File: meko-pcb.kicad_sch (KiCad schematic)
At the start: 75 parts, among them IC1 AS5600-ASOM, IC2 TCAL9538RSVR, J1 GDEY0154D67, J2 MEM2090-00-145-00-A, M1 Motor_DC, Q1 SS8050, Q2 SS8050, Q3 SS8050, Q4 Si1308EDL, SW1 SW_Push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

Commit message: added titles to sheets
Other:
- title: (none) -> ROOT
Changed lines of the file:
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@@
 	(generator_version "9.0")
 	(paper "A3")
+	(title_block
+		(title "ROOT")
+	)
 	(rectangle
 		(start 118.11 86.36)

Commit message: small fixes
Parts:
- added D13: MBR0530, Diode_SMD:D_SOD-123, symbol Diode:MBR0530
- D1: footprint Diode_THT:D_DO-41_SOD81_P3.81mm_Vertical_AnodeUp -> Diode_SMD:D_SMA
- R10, R11: value 10k -> 1.2k
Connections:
- net AUDIO_DATA1: no longer U1.35 (GPIO21)
- net AUDIO_DATA_2: no longer U1.34 (GPIO22)
- net AUDIO_DATA_CLK: now also D13.1 (K); no longer Q2.3 (C)
- net BTN_SIDE_L: now also U1.34 (GPIO22); no longer IC2.5 (P3)
- net BTN_SIDE_R: now also U1.35 (GPIO21); no longer IC2.10 (P7)
- net I2C_1_SCL renamed I2C_SCL
- net I2C_1_SDA renamed I2C_SDA
- new net: D13.2 (A), Q2.3 (C)
- new net PWR_EN3V3AVDD: IC2.10 (P7)
- no-connect marks 6 -> 7
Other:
- sheet power ports: added EN3V3AVDD; removed none

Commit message: fuel gauge ic
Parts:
- C1, C10, C11, C12, C13, C14, C15, C16, C17, C18, C19, C2, C20, C21, C22, C3, C4, C5, C6, C7, C8, C9: footprint (none) -> Capacitor_SMD:C_0402_1005Metric
- IC1: footprint SOIC127P600X175-8N -> AS5600-ASOM:SOIC127P600X175-8N
- IC2: footprint QFN40P180X260X55-16N -> TCAL9538RSVR:QFN40P180X260X55-16N
- J1: footprint FH34SRJ24S05SH99 -> FH34SRJ-24S-0.5SH(99):FH34SRJ24S05SH99
- R1, R12, R13, R14, R15, R2, R3, R4, R5, R6, R7, R8, R9: footprint (none) -> Resistor_SMD:R_0402_1005Metric
- R10, R11: value 1.2k -> 10k; footprint (none) -> Resistor_SMD:R_0402_1005Metric
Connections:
- net AUDIO_SCL is gone; now on net AUDIO_DATA1: U1.15 (GPIO25/ADC2_CH8/DAC_1)
- net AUDIO_SDA is gone; now on net AUDIO_DATA1: U1.16 (GPIO26/ADC2_CH9/DAC_2)
- net AUDIO_DATA_CLK: no longer C7.1, D13.1 (K), SW7.2, U1.23 (GPIO0/BOOT/ADC2_CH1)
- net LED: now also U1.27 (SD_DATA_0/GPIO7); no longer U1.7 (SENSOR_VN/GPIO39/ADC1_CH3)
- net MEM_COM: now also U1.7 (SENSOR_VN/GPIO39/ADC1_CH3); no longer U1.27 (SD_DATA_0/GPIO7)
- net PWR_FUEL_GPOUT: now reaches IC2.5 (P3)
- new net AUDIO_DATA_CLK/BOOT: C7.1, D13.1 (K), SW7.2, U1.23 (GPIO0/BOOT/ADC2_CH1)
- no-connect marks 7 -> 5
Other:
- sheet power ports: added FUEL_GPOUT, FUEL_SCL, FUEL_SDA; removed none
- note added: "addr(dec.):112"
- note added: "addr(dec.):54"
- moved on the sheet: C1, C10, C2, C3, C4, C5, C6, C7, C8, C9, D1, D13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

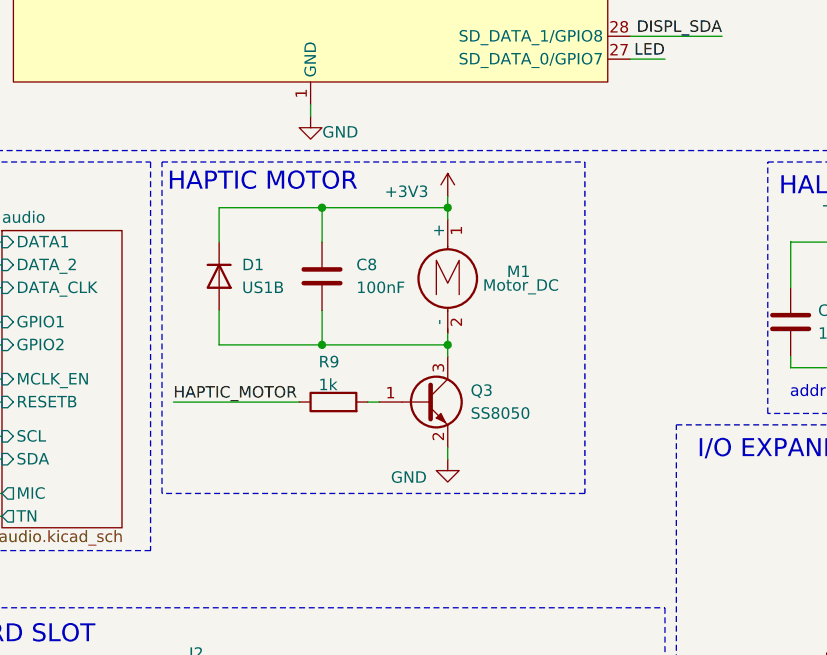
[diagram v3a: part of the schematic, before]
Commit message: added missing 3d models
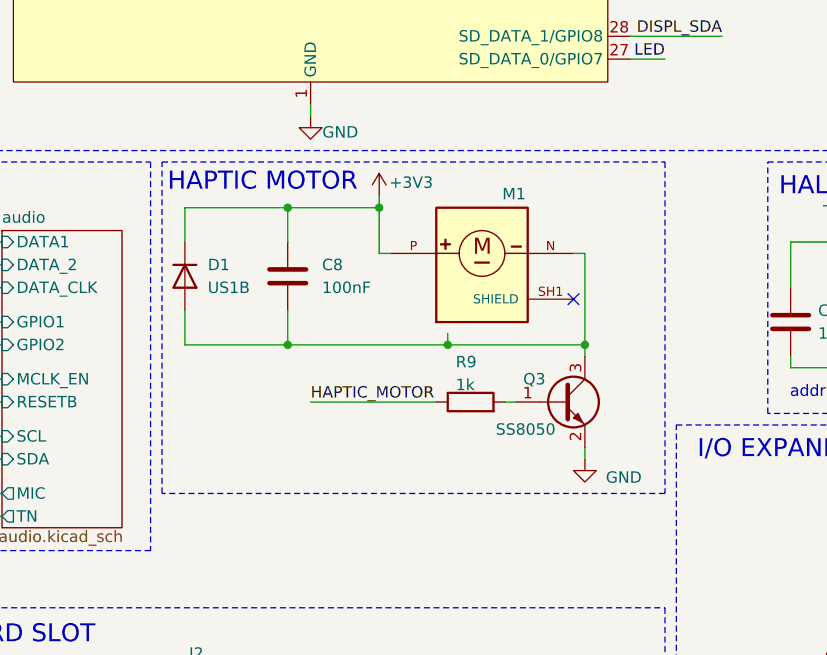
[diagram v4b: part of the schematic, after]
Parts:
- removed M1: Motor_DC, symbol Motor:Motor_DC
- added M1: HD-EMB1204-SM, HD-EMB1204-SM:PUI_HD-EMB1204-SM, symbol HD-EMB1204-SM:HD-EMB1204-SM
- SW1, SW2, SW3, SW4, SW5: footprint (none) -> Button_Switch_SMD:SW_Push_1P1T-MP_NO_Horizontal_Alps_SKRTLAE010
- SW6, SW7: footprint (none) -> Button_Switch_SMD:SW_Push_SPST_NO_Alps_SKRK
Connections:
- net +3V3: now also M1.P
- net at C8.2, D1.2 (A), Q3.3 (C): now also M1.N
- no-connect marks 5 -> 6
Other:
- moved on the sheet: C8, D1, Q3, R9

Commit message: small stuff
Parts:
- added TP19, TP20: TestPoint, TestPoint:TestPoint_Pad_D1.5mm, symbol Connector:TestPoint
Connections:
- net AUDIO_DATA1: now also U1.33 (GPIO19); no longer U1.15 (GPIO25/ADC2_CH8/DAC_1), U1.16 (GPIO26/ADC2_CH9/DAC_2)
- net AUDIO_DATA_2: now also U1.26 (GPIO20)
- net I2C_SCL: now also U1.15 (GPIO25/ADC2_CH8/DAC_1), TP20.1; no longer U1.33 (GPIO19)
- net I2C_SDA: now also U1.16 (GPIO26/ADC2_CH9/DAC_2), TP19.1; no longer U1.26 (GPIO20)
- no-connect marks 6 -> 5
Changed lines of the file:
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@@
 	(text "addr(dec.):112"
 		(exclude_from_sim no)
-		(at 114.554 174.752 0)
+		(at 119.634 172.974 0)
 		(effects
 			(font
@@
 	)
 	(junction
-		(at 82.55 113.03)
-		(diameter 0)
-		(color 0 0 0 0)
-	)
-	(junction
 		(at 64.77 113.03)
 		(diameter 0)
@@
 	)
 	(junction
+		(at 148.59 67.31)
+		(diameter 0)
+		(color 0 0 0 0)
+	)
+	(junction
 		(at 217.17 20.32)
 		(diameter 0)
@@
 	)
 	(junction
-		(at 130.81 115.57)
+		(at 148.59 59.69)
 		(diameter 0)
 		(color 0 0 0 0)
 	)
-	(no_connect
-		(at 257.81 121.92)
+	(junction
+		(at 130.81 115.57)
+		(diameter 0)
+		(color 0 0 0 0)
 	)
 	(no_connect
@@
 	)
 	(no_connect
-		(at 257.81 119.38)
+		(at 259.08 121.92)
 	)
 	(no_connect
@@
 	(wire
 		(pts
+			(xy 259.08 121.92) (xy 270.51 121.92)
+		)
+		(stroke
+			(width 0)
+			(type default)
+		)
+	)
+	(wire
+		(pts
 			(xy 74.93 162.56) (xy 74.93 165.1)
 		)
@@
 	(wire
 		(pts
-			(xy 147.32 67.31) (xy 157.48 67.31)
+			(xy 147.32 67.31) (xy 148.59 67.31)
 		)
 		(stroke
@@
 	(wire
 		(pts
-			(xy 64.77 113.03) (xy 82.55 113.03)
+			(xy 64.77 113.03) (xy 97.79 113.03)
 		)
 		(stroke
@@
 	(wire
 		(pts
-			(xy 102.87 50.8) (xy 113.03 50.8)
+			(xy 102.87 50.8) (xy 116.84 50.8)
 		)
 		(stroke
@@
 	(wire
 		(pts
-			(xy 257.81 121.92) (xy 270.51 121.92)
-		)
-		(stroke
-			(width 0)
-			(type default)
-		)
-	)
-	(wire
-		(pts
 			(xy 67.31 119.38) (xy 81.28 119.38)
 		)
@@
 	(wire
 		(pts
+			(xy 148.59 67.31) (xy 157.48 67.31)
+		)
+		(stroke
+			(width 0)
+			(type default)
+		)
+	)
+	(wire
+		(pts
 			(xy 19.05 157.48) (xy 19.05 158.75)
 		)
@@
 	(wire
 		(pts
-			(xy 102.87 53.34) (xy 113.03 53.34)
-		)
-		(stroke
-			(width 0)
-			(type default)
-		)
-	)
-	(wire
-		(pts
 			(xy 162.56 30.48) (xy 163.83 30.48)
 		)
@@
 	(wire
 		(pts
-			(xy 157.48 59.69) (xy 147.32 59.69)
+			(xy 157.48 59.69) (xy 148.59 59.69)
 		)
 		(stroke
@@
 	(wire
 		(pts
+			(xy 259.08 119.38) (xy 270.51 119.38)
+		)
+		(stroke
+			(width 0)
+			(type default)
+		)
+	)
+	(wire
+		(pts
 			(xy 116.84 60.96) (xy 102.87 60.96)
 		)
@@
 	(wire
 		(pts
-			(xy 257.81 119.38) (xy 270.51 119.38)
+			(xy 83.82 165.1) (xy 93.98 165.1)
 		)
 		(stroke
@@
 	(wire
 		(pts
-			(xy 83.82 165.1) (xy 93.98 165.1)
+			(xy 148.59 59.69) (xy 147.32 59.69)
 		)
 		(stroke
@@
 	(wire
 		(pts
+			(xy 102.87 53.34) (xy 116.84 53.34)
+		)
+		(stroke
+			(width 0)
+			(type default)
+		)
+	)
+	(wire
+		(pts
 			(xy 297.18 154.94) (xy 297.18 153.67)
 		)
@@
 	(wire
 		(pts
-			(xy 82.55 111.76) (xy 82.55 113.03)
-		)
-		(stroke
-			(width 0)
-			(type default)
-		)
-	)
-	(wire
-		(pts
 			(xy 184.15 101.6) (xy 184.15 109.22)
 		)
@@
 	(wire
 		(pts
-			(xy 97.79 113.03) (xy 82.55 113.03)
-		)
-		(stroke
-			(width 0)
-			(type default)
-		)
-	)
-	(wire
-		(pts
 			(xy 252.73 173.99) (xy 252.73 176.53)
 		)
@@
 	(wire
 		(pts
-			(xy 16.51 106.68) (xy 33.02 106.68)
+			(xy 10.16 106.68) (xy 33.02 106.68)
 		)
 		(stroke
@@
 		)
 	)
-	(label "AUDIO_DATA_CLK"
-		(at 16.51 106.68 0)
-		(effects
-			(font
-				(size 1.27 1.27)
-			)
-			(justify left bottom)
-		)
-	)
 	(label "EXP_~{RES}"
 		(at 110.49 154.94 0)
@@
 		)
 	)
-	(label "AUDIO_DATA1"
-		(at 116.84 60.96 180)
-		(effects
-			(font
-				(size 1.27 1.27)
-			)
-			(justify right bottom)
-		)
-	)
 	(label "AUDIO_TN"
 		(at 21.59 132.08 0)
@@
 	)
 	(label "I2C_SCL"
-		(at 113.03 50.8 180)
+		(at 116.84 60.96 180)
 		(effects
 			(font
@@
 		)
 	)
+	(label "AUDIO_DATA_2"
+		(at 116.84 53.34 180)
+		(effects
+			(font
+				(size 1.27 1.27)
+			)
+			(justify right bottom)
+		)
+	)
 	(label "MEM_DAT2"
 		(at 25.4 154.94 0)
@@
 	)
 	(label "I2C_SDA"
-		(at 113.03 53.34 180)
+		(at 116.84 63.5 180)
 		(effects
 			(font
@@
 	)
 	(label "AUDIO_DATA1"
-		(at 116.84 63.5 180)
+		(at 116.84 50.8 180)
 		(effects
 			(font
@@
 		)
 	)
+	(label "AUDIO_DATA_CLK{slash}BOOT"
+		(at 10.16 106.68 0)
+		(effects
+			(font
+				(size 1.27 1.27)
+			)
+			(justify left bottom)
+		)
+	)
 	(label "ESP_EN"
 		(at 330.2 30.48 180)
@@
 	)
 	(symbol
+		(lib_id "Connector:TestPoint")
+		(at 148.59 59.69 0)
+		(unit 1)
+		(exclude_from_sim no)
+		(in_bom yes)
+		(on_board yes)
+		(dnp no)
+		(property "Reference" "TP19"
+			(at 146.558 54.61 0)
+			(effects
+				(font
+					(size 1.27 1.27)
+				)
+				(justify left)
+			)
+		)
+		(property "Value" "TestPoint"
+			(at 151.13 57.6579 0)
+			(effects
+				(font
+					(size 1.27 1.27)
+				)
+				(justify left)
+				(hide yes)
+			)
+		)
+		(property "Footprint" "TestPoint:TestPoint_Pad_D1.5mm"
+			(at 153.67 59.69 0)
+			(effects
+				(font
+					(size 1.27 1.27)
+				)
+				(hide yes)
+			)
+		)
+		(property "Datasheet" "~"
+			(at 153.67 59.69 0)
+			(effects
+				(font
+					(size 1.27 1.27)
+				)
+				(hide yes)
+			)
+		)
+		(property "Description" "test point"
+			(at 148.59 59.69 0)
+			(effects
+				(font
+					(size 1.27 1.27)
+				)
+				(hide yes)
+			)
+		)
+		(pin "1"
+		)
+		(instances
+			(project "meko-pcb"
+				(path "/bdd43acd-23c1-472b-909a-8e24eb60d56d"
+					(reference "TP19")
+					(unit 1)
+				)
+			)
+		)
+	)
+	(symbol
 		(lib_id "TCAL9538RSVR:TCAL9538RSVR")
 		(at 129.54 154.94 0)
@@
 					(unit 1)
 				)
+			)
+		)
+	)
+	(symbol
+		(lib_id "Connector:TestPoint")
+		(at 148.59 67.31 0)
+		(unit 1)
+		(exclude_from_sim no)
+		(in_bom yes)
+		(on_board yes)
+		(dnp no)
+		(property "Reference" "TP20"
+			(at 146.558 62.23 0)
+			(effects
+				(font
+					(size 1.27 1.27)
+				)
+				(justify left)
+			)
+		)
+		(property "Value" "TestPoint"
+			(at 151.13 65.2779 0)
+			(effects
+				(font
+					(size 1.27 1.27)
+				)
+				(justify left)
+				(hide yes)
+			)
+		)
+		(property "Footprint" "TestPoint:TestPoint_Pad_D1.5mm"
+			(at 153.67 67.31 0)
+			(effects
+				(font
+					(size 1.27 1.27)
+				)
+				(hide yes)
+			)
+		)
+		(property "Datasheet" "~"
+			(at 153.67 67.31 0)
+			(effects
+				(font
+					(size 1.27 1.27)
+				)
+				(hide yes)
+			)
+		)
+		(property "Description" "test point"
+			(at 148.59 67.31 0)
+			(effects
+				(font
+					(size 1.27 1.27)
+				)
+				(hide yes)
+			)
+		)
+		(pin "1"
+		)
+		(instances
+			(project "meko-pcb"
+				(path "/bdd43acd-23c1-472b-909a-8e24eb60d56d"
+					(reference "TP20")
+					(unit 1)
+				)

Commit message: added models
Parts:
- D2: footprint LED_SMD:LED_SK6805_PLCC4_2.4x2.7mm_P1.3mm -> sk6805-ec14:sk6805ec14
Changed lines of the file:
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@@
 			)
 		)
-		(property "Footprint" "LED_SMD:LED_SK6805_PLCC4_2.4x2.7mm_P1.3mm"
+		(property "Footprint" "sk6805-ec14:sk6805ec14"
 			(at 173.99 73.66 0)
 			(effects

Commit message: started layout
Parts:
- J1: footprint FH34SRJ-24S-0.5SH(99):FH34SRJ24S05SH99 -> FH34SRJ-24S-0.5SH(99):FH34SRJ24S05SH99-disp
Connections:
- net AUDIO_DATA1: now also U1.26 (GPIO20); no longer U1.33 (GPIO19)
- net AUDIO_DATA_2: now also U1.27 (SD_DATA_0/GPIO7); no longer U1.26 (GPIO20)
- net LED: now also U1.33 (GPIO19); no longer U1.27 (SD_DATA_0/GPIO7)
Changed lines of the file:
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@@
 	(wire
 		(pts
-			(xy 115.57 55.88) (xy 102.87 55.88)
+			(xy 116.84 55.88) (xy 102.87 55.88)
 		)
 		(stroke
@@
 	(wire
 		(pts
-			(xy 22.86 66.04) (xy 31.75 66.04)
+			(xy 17.78 66.04) (xy 31.75 66.04)
 		)
 		(stroke
@@
 	(wire
 		(pts
-			(xy 113.03 78.74) (xy 102.87 78.74)
+			(xy 116.84 78.74) (xy 102.87 78.74)
 		)
 		(stroke
@@
 	(wire
 		(pts
-			(xy 115.57 58.42) (xy 102.87 58.42)
+			(xy 116.84 58.42) (xy 102.87 58.42)
 		)
 		(stroke
@@
 	(wire
 		(pts
-			(xy 106.68 81.28) (xy 102.87 81.28)
+			(xy 116.84 81.28) (xy 102.87 81.28)
 		)
 		(stroke
@@
 	(wire
 		(pts
-			(xy 24.13 40.64) (xy 31.75 40.64)
+			(xy 17.78 40.64) (xy 31.75 40.64)
 		)
 		(stroke
@@
 	(wire
 		(pts
-			(xy 21.59 71.12) (xy 31.75 71.12)
+			(xy 17.78 71.12) (xy 31.75 71.12)
 		)
 		(stroke
@@
 	(wire
 		(pts
-			(xy 21.59 73.66) (xy 31.75 73.66)
+			(xy 17.78 73.66) (xy 31.75 73.66)
 		)
 		(stroke
@@
 	(wire
 		(pts
-			(xy 20.32 60.96) (xy 31.75 60.96)
+			(xy 17.78 60.96) (xy 31.75 60.96)
 		)
 		(stroke
@@
 	(wire
 		(pts
-			(xy 114.3 66.04) (xy 102.87 66.04)
+			(xy 116.84 66.04) (xy 102.87 66.04)
 		)
 		(stroke
@@
 	(wire
 		(pts
-			(xy 22.86 63.5) (xy 31.75 63.5)
+			(xy 17.78 63.5) (xy 31.75 63.5)
 		)
 		(stroke
@@
 	)
 	(label "BTN_VOL_UP"
-		(at 20.32 60.96 0)
+		(at 17.78 60.96 0)
 		(effects
 			(font
@@
 	)
 	(label "DISPL_SDA"
-		(at 113.03 78.74 180)
+		(at 116.84 78.74 180)
 		(effects
 			(font
@@
 	)
 	(label "BTN_PWR"
-		(at 22.86 63.5 0)
+		(at 17.78 63.5 0)
 		(effects
 			(font
@@
 	)
 	(label "AUDIO_MIC"
-		(at 21.59 71.12 0)
+		(at 17.78 71.12 0)
 		(effects
 			(font
@@
 	)
 	(label "LED"
-		(at 106.68 81.28 180)
+		(at 116.84 50.8 180)
 		(effects
 			(font
@@
 	)
 	(label "HAL_OUT"
-		(at 22.86 66.04 0)
+		(at 17.78 66.04 0)
 		(effects
 			(font
@@
 	)
 	(label "BTN_SIDE_L"
-		(at 115.57 58.42 180)
+		(at 116.84 58.42 180)
 		(effects
 			(font
@@
 	)
 	(label "AUDIO_DATA_2"
-		(at 116.84 53.34 180)
+		(at 116.84 81.28 180)
 		(effects
 			(font
@@
 	)
 	(label "MEM_COM"
-		(at 21.59 73.66 0)
+		(at 17.78 73.66 0)
 		(effects
 			(font
@@
 	)
 	(label "BTN_SIDE_R"
-		(at 115.57 55.88 180)
+		(at 116.84 55.88 180)
 		(effects
 			(font
@@
 	)
 	(label "DISPL_SCL"
-		(at 114.3 66.04 180)
+		(at 116.84 66.04 180)
 		(effects
 			(font
@@
 	)
 	(label "EXP_~{INT}"
-		(at 24.13 40.64 0)
+		(at 17.78 40.64 0)
 		(effects
 			(font
@@
 	)
 	(label "AUDIO_DATA1"
-		(at 116.84 50.8 180)
+		(at 116.84 53.34 180)
 		(effects
 			(font
@@
 			)
 		)
-		(property "Footprint" "FH34SRJ-24S-0.5SH(99):FH34SRJ24S05SH99"
+		(property "Footprint" "FH34SRJ-24S-0.5SH(99):FH34SRJ24S05SH99-disp"
 			(at 283.21 206.68 0)
 			(effects
@@
 			)
 		)
-		(property "Datasheet" "https://v4.cecdn.yun300.cn/100001_1909185148/GDEY0154D67-new.pdf"
+		(property "Datasheet" "https://www.good-display.com/public/html/pdfjs/viewer/viewernew.html?file=https://v4.cecdn.yun300.cn/100001_1909185148/GDEY0154D67-new.pdf"
 			(at 283.21 306.68 0)
 			(effects

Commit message: layout
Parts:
- removed TP7: TestPoint, TestPoint:TestPoint_Pad_D1.5mm, symbol Connector:TestPoint
- added C60: 4.7uF, Capacitor_SMD:C_0402_1005Metric, symbol Device:C
- added C61: 100nF, Capacitor_SMD:C_0402_1005Metric, symbol Device:C
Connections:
- net +3V3: now also C60.2, C61.1
- net GND: now also C60.1, C61.2
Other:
- sheet power ports: added none; removed EN3V3MCLK
